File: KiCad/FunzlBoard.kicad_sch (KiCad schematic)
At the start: 65 parts, among them SW1 SW_MEC_5E, SW2 SW_MEC_5E, SW3 SW_MEC_5E, SW4 SW_MEC_5E, U1 ESP32-C3_SUPERMINI_SMD, U2 ADS7828, U3 MCP23017_SO

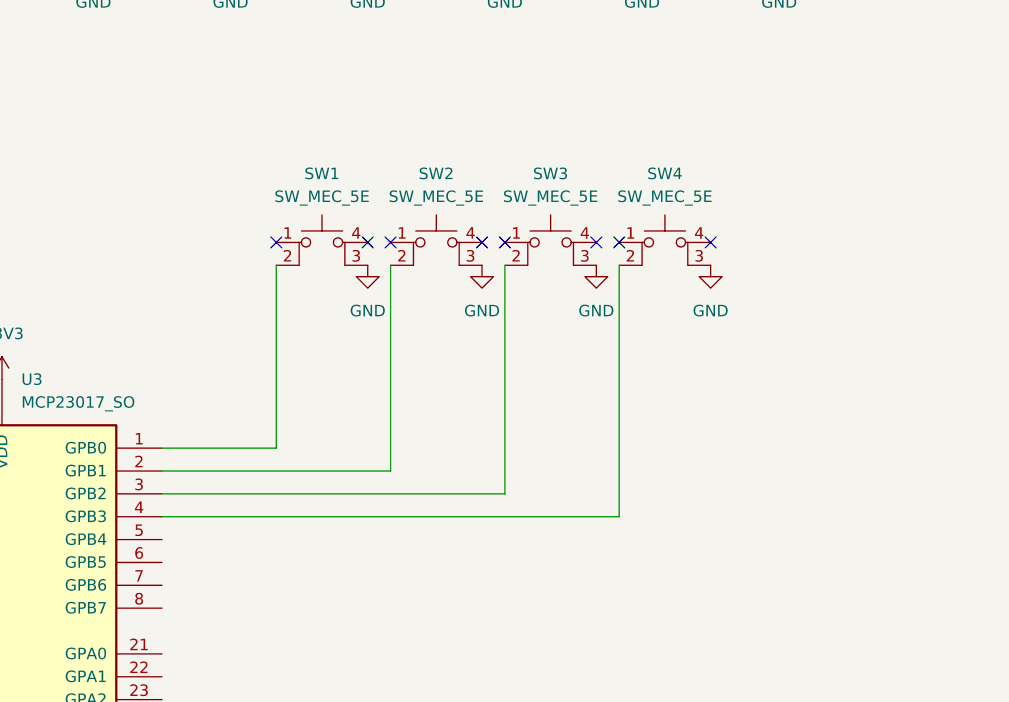
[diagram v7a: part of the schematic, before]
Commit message: Add DIP Switch to PCB
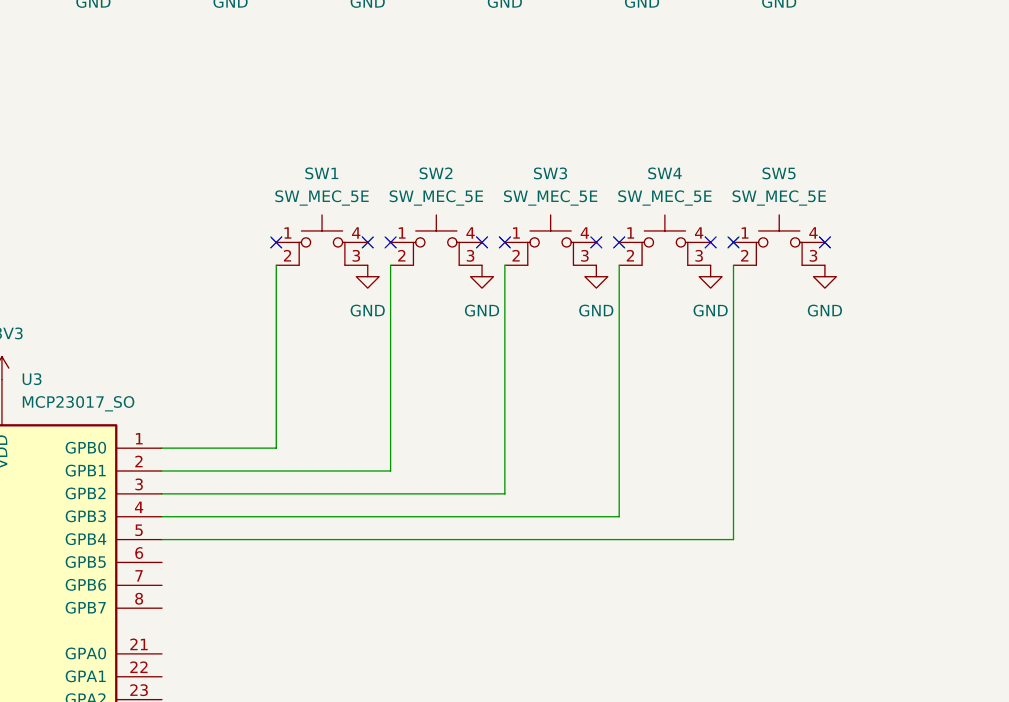
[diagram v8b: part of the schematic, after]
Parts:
- added SW5: SW_MEC_5E, Button_Switch_THT:SW_PUSH_6mm_H13mm, symbol Switch:SW_MEC_5E
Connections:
- net GND: now also SW5.3 (K)
- net at U3.5 (GPB4): now also SW5.2
- no-connect marks 11 -> 13
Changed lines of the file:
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@@
 	)
 	(no_connect
+		(at 340.36 100.33)
+	)
+	(no_connect
 		(at 302.26 100.33)
 	)
@@
 	)
 	(no_connect
+		(at 330.2 100.33)
+	)
+	(no_connect
 		(at 231.14 140.97)
 	)
@@
 	(wire
 		(pts
+			(xy 266.7 133.35) (xy 330.2 133.35)
+		)
+		(stroke
+			(width 0)
+			(type default)
+		)
+	)
+	(wire
+		(pts
 			(xy 185.42 135.89) (xy 173.99 135.89)
 		)
@@
 	(wire
 		(pts
+			(xy 330.2 102.87) (xy 330.2 133.35)
+		)
+		(stroke
+			(width 0)
+			(type default)
+		)
+	)
+	(wire
+		(pts
 			(xy 173.99 135.89) (xy 173.99 106.68)
 		)
@@
 	)
 	(symbol
+		(lib_id "Switch:SW_MEC_5E")
+		(at 335.28 102.87 0)
+		(unit 1)
+		(exclude_from_sim no)
+		(in_bom yes)
+		(on_board yes)
+		(dnp no)
+		(fields_autoplaced yes)
+		(property "Reference" "SW5"
+			(at 335.28 92.71 0)
+			(effects
+				(font
+					(size 1.27 1.27)
+				)
+			)
+		)
+		(property "Value" "SW_MEC_5E"
+			(at 335.28 95.25 0)
+			(effects
+				(font
+					(size 1.27 1.27)
+				)
+			)
+		)
+		(property "Footprint" "Button_Switch_THT:SW_PUSH_6mm_H13mm"
+			(at 335.28 95.25 0)
+			(effects
+				(font
+					(size 1.27 1.27)
+				)
+				(hide yes)
+			)
+		)
+		(property "Datasheet" "http://www.apem.com/int/index.php?controller=attachment&id_attachment=1371"
+			(at 335.28 95.25 0)
+			(effects
+				(font
+					(size 1.27 1.27)
+				)
+				(hide yes)
+			)
+		)
+		(property "Description" "MEC 5E single pole normally-open tactile switch"
+			(at 335.28 102.87 0)
+			(effects
+				(font
+					(size 1.27 1.27)
+				)
+				(hide yes)
+			)
+		)
+		(pin "2"
+		)
+		(pin "4"
+		)
+		(pin "1"
+		)
+		(pin "3"
+		)
+		(instances
+			(project "FunzlBoard"
+				(path "/969bb173-34d7-4b46-8a59-72ed8ea1ad7c"
+					(reference "SW5")
+					(unit 1)
+				)
+			)
+		)
+	)
+	(symbol
 		(lib_id "power:+3V3")
 		(at 172.72 99.06 0)
@@
 					(unit 1)
 				)
+			)
+		)
+	)
+	(symbol
+		(lib_id "power:GND")
+		(at 340.36 102.87 0)
+		(unit 1)
+		(exclude_from_sim no)
+		(in_bom yes)
+		(on_board yes)
+		(dnp no)
+		(fields_autoplaced yes)
+		(property "Reference" "#PWR0117"
+			(at 340.36 109.22 0)
+			(effects
+				(font
+					(size 1.27 1.27)
+				)
+				(hide yes)
+			)
+		)
+		(property "Value" "GND"
+			(at 340.36 107.95 0)
+			(effects
+				(font
+					(size 1.27 1.27)
+				)
+			)
+		)
+		(property "Footprint" ""
+			(at 340.36 102.87 0)
+			(effects
+				(font
+					(size 1.27 1.27)
+				)
+				(hide yes)
+			)
+		)
+		(property "Datasheet" ""
+			(at 340.36 102.87 0)
+			(effects
+				(font
+					(size 1.27 1.27)
+				)
+				(hide yes)
+			)
+		)
+		(property "Description" "Power symbol creates a global label with name \"GND\" , ground"
+			(at 340.36 102.87 0)
+			(effects
+				(font
+					(size 1.27 1.27)
+				)
+				(hide yes)
+			)
+		)
+		(pin "1"
+		)
+		(instances
+			(project "FunzlBoard"
+				(path "/969bb173-34d7-4b46-8a59-72ed8ea1ad7c"
+					(reference "#PWR0117")
+					(unit 1)
+				)
